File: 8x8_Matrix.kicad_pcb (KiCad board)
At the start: 2 copper layers, 20 x 20 mm, 64 parts

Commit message: Finished PCB front
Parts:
- moved D49 73.0 mm to (131.5, 105.0), turned to 180 degrees
- moved D19 69.7 mm to (136.5, 95.0), turned to 180 degrees
- moved D48 68.9 mm to (131.5, 102.5), turned to 90 degrees
- moved D18 68.1 mm to (134.0, 95.0), turned to 180 degrees
- moved D29 67.0 mm to (139.0, 97.4), turned to 90 degrees
- moved D17 66.4 mm to (131.5, 95.0), turned to 180 degrees
- moved D47 62.6 mm to (134.0, 102.5), turned to 90 degrees
- moved D16 60.8 mm to (131.5, 92.5), turned to 90 degrees
- moved D28 60.7 mm to (141.5, 97.4), turned to 90 degrees
- moved D59 60.6 mm to (144.0, 107.5), turned to 90 degrees
- moved D39 59.4 mm to (146.5, 100.0), turned to 180 degrees
- moved D9 58.4 mm to (149.0, 92.5), turned to 90 degrees
- moved D38 57.9 mm to (144.0, 100.0), turned to 180 degrees
- moved D37 55.1 mm to (141.5, 100.0), turned to 180 degrees
- moved D46 55.0 mm to (136.5, 102.5), turned to 90 degrees
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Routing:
- net +5V: track 0.00 -> 120.4 mm
- net Net-(D54-Pad1): track 0.00 -> 2.07 mm
- net Net-(D17-Pad1): track 0.00 -> 1.99 mm
- net Net-(D7-Pad1): track 0.00 -> 1.97 mm
- net Net-(D63-Pad1): track 0.00 -> 1.97 mm
- net Net-(D62-Pad1): track 0.00 -> 1.97 mm
- net Net-(D61-Pad1): track 0.00 -> 1.97 mm
- net Net-(D60-Pad1): track 0.00 -> 1.97 mm
- net Net-(D6-Pad1): track 0.00 -> 1.97 mm
- net Net-(D59-Pad1): track 0.00 -> 1.97 mm
- net Net-(D58-Pad1): track 0.00 -> 1.97 mm
- net Net-(D57-Pad1): track 0.00 -> 1.97 mm
- net Net-(D55-Pad1): track 0.00 -> 1.97 mm
- net Net-(D53-Pad1): track 0.00 -> 1.97 mm
- net Net-(D52-Pad1): track 0.00 -> 1.97 mm
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- added copper zone on B.Cu, net GND
- added copper zone on F.Cu, net GND

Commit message: Finished PCB Back
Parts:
- added ?: , , F.Cu at (132.5, 99.0)
- added ?: , , F.Cu at (147.5, 95.5)
- added ?: , easyeda:PADPAD, F.Cu at (132.5, 94.2)
- added ?: , , F.Cu at (147.5, 102.5)
- added ?: , , F.Cu at (147.5, 99.0)
- added ?: , , F.Cu at (132.5, 102.5)
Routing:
- net +5V: track 120.4 -> 167.2 mm, vias 0 -> 12
- net DIN: track 0.72 -> 23.4 mm
- net DOUT: track 0.65 -> 10.7 mm
- net GND: vias 29 -> 18

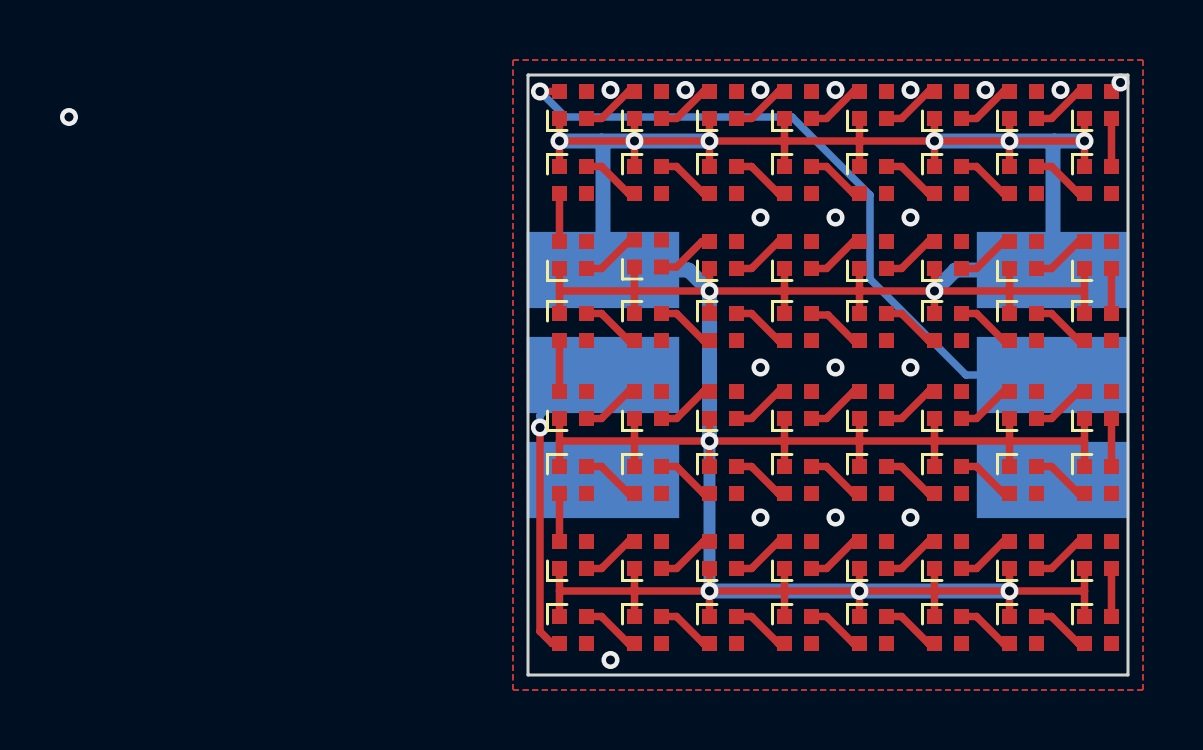
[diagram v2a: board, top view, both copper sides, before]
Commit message: Optimized PCB and added silkscreen
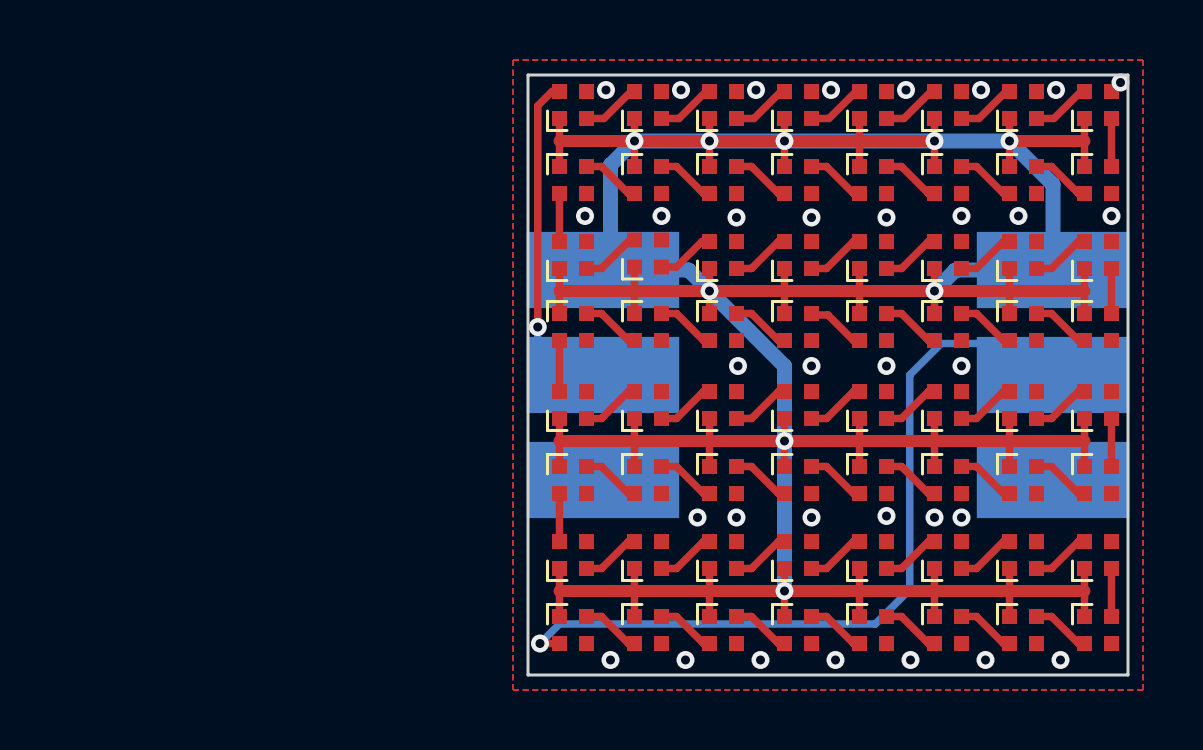
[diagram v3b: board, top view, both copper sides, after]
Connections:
- ? pad 1: DOUT -> DIN
- ? pad 1: DIN -> DOUT
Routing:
- net DOUT: track 10.7 -> 26.5 mm
- net DIN: track 23.4 -> 14.0 mm
- net +5V: track 167.2 -> 159.2 mm, vias 12 -> 9
- net GND: vias 18 -> 33
- net (no net): vias 1 -> 0
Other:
- board text added: "2022/05"
- board text added: "5V"
- board text added: "DIN"
- board text added: "DOUT"
- board text added: "GND"
- board text added: "JLCJLCJLCJLC"
- board text added: "REV1.0"
- board text added: "SK6805EC15 Matrix"
- board text added: "© foorschtbar"
